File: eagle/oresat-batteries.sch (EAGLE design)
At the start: 73 parts, among them IC1 74AHC1G08DBV, U1 TCAN330, U2 STM32F042K6, U3 ADP5062, X1 16MHz

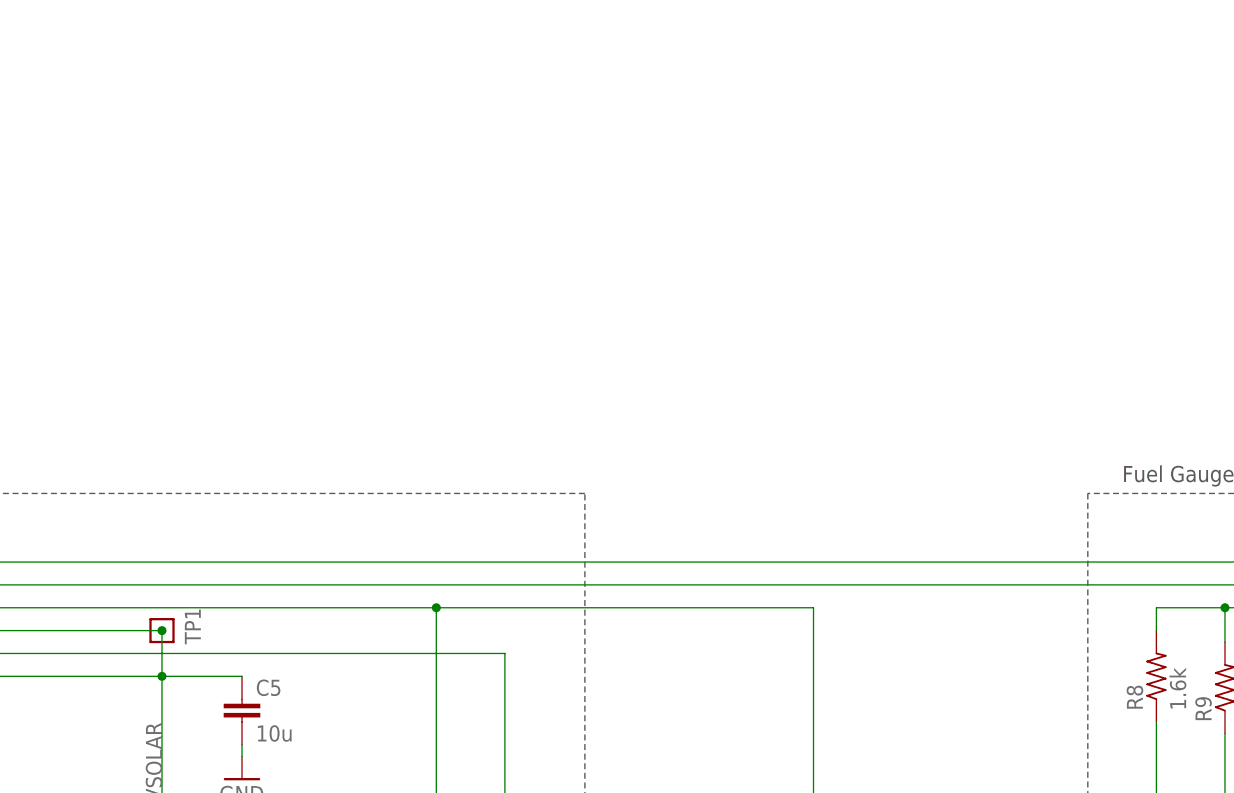
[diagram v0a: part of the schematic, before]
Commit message: Added 3.3V switching power supply
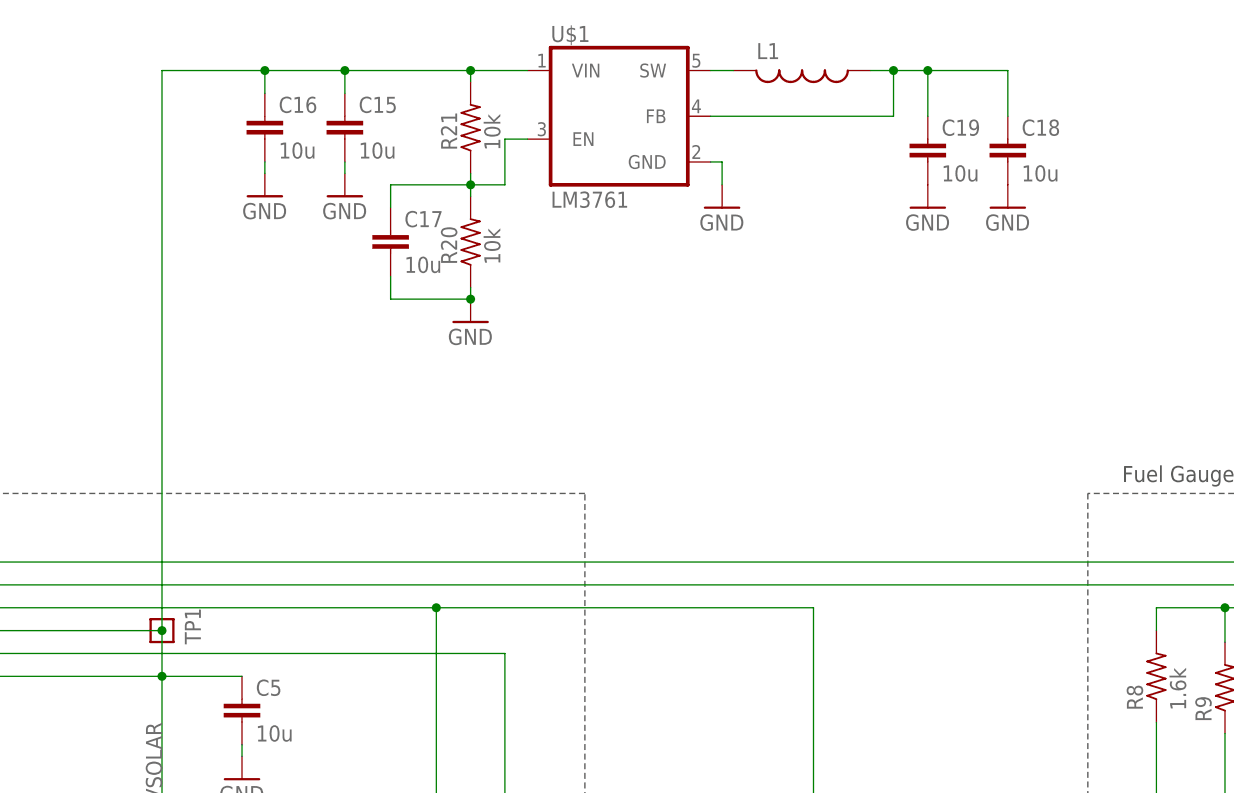
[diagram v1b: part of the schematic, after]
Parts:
- added C15, C16, C17, C18, C19: 10u, rcl:C-EUC0805
- added L1: (no value), rcl:L-USL2012C
- added R20, R21: 10k, rcl:R-US_R0603
- added U$1: LM3761, oresat-batteries:LM3761
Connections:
- new net N$1: L1.2, U$1.SW
- new net N$3: C18.1, C19.1, L1.1, U$1.FB
- new net N$7: C17.1, R20.2, R21.1, U$1.EN
- net GND: now also C15.2, C16.2, C17.2, C18.2, C19.2, R20.1, U$1.GND
- net VSOLAR: now also C15.1, C16.1, R21.2, U$1.VIN
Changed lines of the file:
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@@
 <part name="GND35" library="supply1" deviceset="GND" device=""/>
 <part name="TP5" library="oresat-batteries" deviceset="TP" device=""/>
+<part name="U$1" library="oresat-batteries" deviceset="LM3761" device=""/>
+<part name="C15" library="rcl" deviceset="C-EU" device="C0805" value="10u"/>
+<part name="C16" library="rcl" deviceset="C-EU" device="C0805" value="10u"/>
+<part name="GND36" library="supply1" deviceset="GND" device=""/>
+<part name="GND37" library="supply1" deviceset="GND" device=""/>
+<part name="C17" library="rcl" deviceset="C-EU" device="C0805" value="10u"/>
+<part name="R20" library="rcl" deviceset="R-US_" device="R0603" value="10k"/>
+<part name="R21" library="rcl" deviceset="R-US_" device="R0603" value="10k"/>
+<part name="GND38" library="supply1" deviceset="GND" device=""/>
+<part name="GND39" library="supply1" deviceset="GND" device=""/>
+<part name="C18" library="rcl" deviceset="C-EU" device="C0805" value="10u"/>
+<part name="C19" library="rcl" deviceset="C-EU" device="C0805" value="10u"/>
+<part name="GND40" library="supply1" deviceset="GND" device=""/>
+<part name="GND41" library="supply1" deviceset="GND" device=""/>
+<part name="L1" library="rcl" deviceset="L-US" device="L2012C"/>
 </parts>
 <sheets>
@@
 <attribute name="NAME" x="74.93" y="237.49" size="1.778" layer="95"/>
 </instance>
+<instance part="U$1" gate="G$1" x="184.15" y="342.9"/>
+<instance part="C15" gate="G$1" x="153.67" y="342.9"/>
+<instance part="C16" gate="G$1" x="144.78" y="342.9"/>
+<instance part="GND36" gate="1" x="144.78" y="334.01"/>
+<instance part="GND37" gate="1" x="153.67" y="334.01"/>
+<instance part="C17" gate="G$1" x="158.75" y="330.2"/>
+<instance part="R20" gate="G$1" x="167.64" y="328.93" smashed="yes" rot="R90">
+<attribute name="NAME" x="166.1414" y="326.39" size="1.778" layer="95" rot="R90"/>
+<attribute name="VALUE" x="170.942" y="326.39" size="1.778" layer="96" rot="R90"/>
+</instance>
+<instance part="R21" gate="G$1" x="167.64" y="341.63" smashed="yes" rot="R90">
+<attribute name="NAME" x="166.1414" y="339.09" size="1.778" layer="95" rot="R90"/>
+<attribute name="VALUE" x="170.942" y="339.09" size="1.778" layer="96" rot="R90"/>
+</instance>
+<instance part="GND38" gate="1" x="167.64" y="320.04"/>
+<instance part="GND39" gate="1" x="195.58" y="332.74"/>
+<instance part="C18" gate="G$1" x="227.33" y="340.36"/>
+<instance part="C19" gate="G$1" x="218.44" y="340.36"/>
+<instance part="GND40" gate="1" x="218.44" y="332.74"/>
+<instance part="GND41" gate="1" x="227.33" y="332.74"/>
+<instance part="L1" gate="G$1" x="204.47" y="347.98" rot="R270"/>
 </instances>
 <busses>
@@
 <pinref part="R19" gate="G$1" pin="1"/>
 <pinref part="GND35" gate="1" pin="GND"/>
+</segment>
+<segment>
+<pinref part="C16" gate="G$1" pin="2"/>
+<pinref part="GND36" gate="1" pin="GND"/>
+<wire x1="144.78" y1="336.55" x2="144.78" y2="337.82" width="0.1524" layer="91"/>
+</segment>
+<segment>
+<pinref part="C15" gate="G$1" pin="2"/>
+<pinref part="GND37" gate="1" pin="GND"/>
+<wire x1="153.67" y1="336.55" x2="153.67" y2="337.82" width="0.1524" layer="91"/>
+</segment>
+<segment>
+<pinref part="R20" gate="G$1" pin="1"/>
+<pinref part="GND38" gate="1" pin="GND"/>
+<wire x1="167.64" y1="323.85" x2="167.64" y2="322.58" width="0.1524" layer="91"/>
+<pinref part="C17" gate="G$1" pin="2"/>
+<wire x1="167.64" y1="322.58" x2="158.75" y2="322.58" width="0.1524" layer="91"/>
+<wire x1="158.75" y1="322.58" x2="158.75" y2="325.12" width="0.1524" layer="91"/>
+<junction x="167.64" y="322.58"/>
+</segment>
+<segment>
+<pinref part="C19" gate="G$1" pin="2"/>
+<pinref part="GND40" gate="1" pin="GND"/>
+</segment>
+<segment>
+<pinref part="C18" gate="G$1" pin="2"/>
+<pinref part="GND41" gate="1" pin="GND"/>
+</segment>
+<segment>
+<pinref part="GND39" gate="1" pin="GND"/>
+<wire x1="195.58" y1="335.28" x2="195.58" y2="337.82" width="0.1524" layer="91"/>
+<pinref part="U$1" gate="G$1" pin="GND"/>
+<wire x1="195.58" y1="337.82" x2="194.31" y2="337.82" width="0.1524" layer="91"/>
 </segment>
 </net>
@@
 <junction x="81.28" y="265.43"/>
 <wire x1="81.28" y1="265.43" x2="81.28" y2="280.67" width="0.1524" layer="91"/>
+<wire x1="133.35" y1="285.75" x2="133.35" y2="347.98" width="0.3048" layer="91"/>
+<pinref part="U$1" gate="G$1" pin="VIN"/>
+<pinref part="C16" gate="G$1" pin="1"/>
+<wire x1="173.99" y1="347.98" x2="167.64" y2="347.98" width="0.3048" layer="91"/>
+<wire x1="167.64" y1="347.98" x2="153.67" y2="347.98" width="0.3048" layer="91"/>
+<wire x1="153.67" y1="347.98" x2="144.78" y2="347.98" width="0.3048" layer="91"/>
+<wire x1="144.78" y1="347.98" x2="144.78" y2="345.44" width="0.1524" layer="91"/>
+<pinref part="C15" gate="G$1" pin="1"/>
+<wire x1="153.67" y1="347.98" x2="153.67" y2="345.44" width="0.1524" layer="91"/>
+<junction x="153.67" y="347.98"/>
+<pinref part="R21" gate="G$1" pin="2"/>
+<wire x1="167.64" y1="347.98" x2="167.64" y2="346.71" width="0.1524" layer="91"/>
+<junction x="167.64" y="347.98"/>
+<wire x1="133.35" y1="347.98" x2="144.78" y2="347.98" width="0.1524" layer="91"/>
+<junction x="144.78" y="347.98"/>
 </segment>
 </net>
@@
 </segment>
 </net>
+<net name="N$1" class="0">
+<segment>
+<pinref part="U$1" gate="G$1" pin="SW"/>
+<pinref part="L1" gate="G$1" pin="2"/>
+<wire x1="194.31" y1="347.98" x2="196.85" y2="347.98" width="0.1524" layer="91"/>
+</segment>
+</net>
+<net name="N$3" class="0">
+<segment>
+<pinref part="U$1" gate="G$1" pin="FB"/>
+<wire x1="194.31" y1="342.9" x2="214.63" y2="342.9" width="0.1524" layer="91"/>
+<wire x1="214.63" y1="342.9" x2="214.63" y2="347.98" width="0.1524" layer="91"/>
+<pinref part="L1" gate="G$1" pin="1"/>
+<wire x1="214.63" y1="347.98" x2="212.09" y2="347.98" width="0.1524" layer="91"/>
+<wire x1="214.63" y1="347.98" x2="218.44" y2="347.98" width="0.1524" layer="91"/>
+<junction x="214.63" y="347.98"/>
+<pinref part="C19" gate="G$1" pin="1"/>
+<wire x1="218.44" y1="347.98" x2="218.44" y2="342.9" width="0.1524" layer="91"/>
+<wire x1="218.44" y1="347.98" x2="227.33" y2="347.98" width="0.1524" layer="91"/>
+<junction x="218.44" y="347.98"/>
+<pinref part="C18" gate="G$1" pin="1"/>
+<wire x1="227.33" y1="347.98" x2="227.33" y2="342.9" width="0.1524" layer="91"/>
+</segment>
+</net>
+<net name="N$7" class="0">
+<segment>
+<pinref part="R21" gate="G$1" pin="1"/>
+<pinref part="R20" gate="G$1" pin="2"/>
+<wire x1="167.64" y1="336.55" x2="167.64" y2="335.28" width="0.1524" layer="91"/>
+<pinref part="C17" gate="G$1" pin="1"/>
+<wire x1="167.64" y1="335.28" x2="167.64" y2="334.01" width="0.1524" layer="91"/>
+<wire x1="158.75" y1="332.74" x2="158.75" y2="335.28" width="0.1524" layer="91"/>
+<wire x1="158.75" y1="335.28" x2="167.64" y2="335.28" width="0.1524" layer="91"/>
+<junction x="167.64" y="335.28"/>
+<wire x1="167.64" y1="335.28" x2="171.45" y2="335.28" width="0.1524" layer="91"/>
+<wire x1="171.45" y1="335.28" x2="171.45" y2="340.36" width="0.1524" layer="91"/>
+<pinref part="U$1" gate="G$1" pin="EN"/>
+<wire x1="171.45" y1="340.36" x2="173.99" y2="340.36" width="0.1524" layer="91"/>
+</segment>
+</net>

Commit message: First cleanup of batteries post-Austin going to NASA. Austiiiiinnnnnnnnn, come backgit diff ../design.mdn111git diff ../design.mdn./run More sane two sheet layout on schematic, cleaned up in and out arrays but it needs more thought. New OreSat card board and connector.
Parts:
- removed C12, C13: 100n, rcl:C-EUC0603
- removed C15, C19: 10u, rcl:C-EUC0805
- removed CF1: ORESAT-CONNECTOR-40PIN, low-gain-radio:ORESAT-CONNECTOR-40PIN
- removed CF2: 2MM-RA-1X8, oresat-batteries:2MM-RA-1X8
- removed DEBUG_DNP: (no value), pinhead:PINHD-2X8
- removed L1: (no value), rcl:L-USL2012C
- removed LED1: DNP/GRN, led:LEDCHIPLED_0603
- removed U$1: LM3761, oresat-batteries:LM3761
- removed U$10, U$11, U$12, U$15, U$16, U$17, U$18, U$19, U$22, U$23, U$25, U$26, U$27, U$28, U$29, U$4, U$8, U$9: TP, oresat-batteries:TP
- removed U$13, U$14, U$20: CSD16340Q3, oresat-batteries:CSD16340Q3
- removed U$2: BQ2970, oresat-batteries:BQ2970
- removed U$21: 4.19, oresat-batteries:RES_HEATER
- removed U$3: 2AHBATT, oresat-batteries:2AHBATT
- removed U$5: STC3100LST, oresat-batteries:STC3100LST
- added B1: 2AHBATT, oresat-batteries:2AHBATT
- added C22: 100n, rcl_custom:C-EU0402-B-NOSILK
- added C25: 22u, oresat-rcl:C-EU0805-B-NOSILK
- added CARD: ORESAT-CARD-V0.5, oresat-card:ORESAT-CARD-V0.5
- added D1, D3: GREEN, SparkFun-LED:LED-GREEN0603
- added F1: 2016L200PR, F-LITTELFUSE-2016L-SERIES-PTC:F-LITTELFUSE-2016L-SERIES-PTC
- added F2: 2016L500DR, F-LITTELFUSE-2016L-SERIES-PTC:F-LITTELFUSE-2016L-SERIES-PTC
- added H1, H2, H3, H4: STAND-OFFTIGHT, SparkFun-Hardware:STAND-OFFTIGHT
- added J5: (no value), SparkFun-Connectors:6_PIN_SERIAL_TARGETSILK
- added J6: J-SAMTEC-TFM-120-X1-XXX-D-RA, J-Samtec-TFM-120-X1-XXX-D-RA:J-SAMTEC-TFM-120-X1-XXX-D-RA
- added J7: 1.27MM-SWD-CONNECTOR, J-CNC-3220-10-0100-00-ARM-SWD-port:1.27MM-SWD-CONNECTOR
- added JP8: (no value), pinhead:PINHD-1X2
- added L3: 1.5 uH, L-Coilcraft-XFL4020:L-COILCRAFT-XFL4020
- added Q1, Q2, Q7: CSD16340Q3, oresat-batteries:CSD16340Q3
- added Q3, Q4, Q5, Q6: TPN4R712MD, tpn4r712md-pmosfet:TPN4R712MD
- added R22, R23, R24, R25: 470k, rcl:R-US_R0603
- added R26, R28, R29: 10k, rcl:R-US_R0603
- added TP10, TP11, TP12, TP13, TP14, TP16, TP17, TP20, TP6, TP7, TP8, TP9: TP, oresat-batteries:TP
- added TP15: TEST-POINT, Tova:TEST-POINT
- added U10, U12, U13, U9: LTC4412, ltc4412:LTC4412
- added U11: MAX17055, max17055:MAX17055
- added U4, U5, U7, U8: LTC4411, ltc4411:LTC4411
- added U6: STM32F042K6, STM32F042K:STM32F042K6
- C10: value 100n -> .1u
- C11: value 100n -> 20p; device rcl:C-EUC0603 -> rcl_custom:C-EU0402-B-NOSILK; DIS (none) -> Digi-Key; DPN (none) -> 1276-6601-1-ND; MFR (none) -> Samsung; MPN (none) -> CL05C200JB51PNC
- C14: value .1u -> 22u; device rcl:C-EUC0603 -> oresat-rcl:C-EU0603-B-NOSILK; DIS (none) -> Digi-Key; DPN (none) -> 1276-1001-1-ND; MFR (none) -> Samsung; MPN (none) -> CL05B104KO5NNNC
- C16: value 10u -> 20p; device rcl:C-EUC0805 -> rcl_custom:C-EU0402-B-NOSILK; DIS (none) -> Digi-Key; DPN (none) -> 1276-6601-1-ND; MFR (none) -> Samsung; MPN (none) -> CL05C200JB51PNC
- C17, C5: value 10u -> 100n; device rcl:C-EUC0805 -> rcl_custom:C-EU0402-B-NOSILK; DIS (none) -> Digi-Key; DPN (none) -> 1276-1001-1-ND; MFR (none) -> Samsung; MPN (none) -> CL05B104KO5NNNC
- C18: value 10u -> 22u; device rcl:C-EUC0805 -> oresat-rcl:C-EU0805-B-NOSILK
- C2: value 22u -> .47u; device rcl:C-EUC1206 -> rcl:C-EUC0603
- C3: value 22u -> 100n; device rcl:C-EUC1206 -> rcl_custom:C-EU0402-B-NOSILK; DIS (none) -> Digi-Key; DPN (none) -> 1276-1001-1-ND; MFR (none) -> Samsung; MPN (none) -> CL05B104KO5NNNC
- C4: value 10n -> 10u; device rcl:C-EUC0603 -> oresat-rcl:C-EU0603-B-NOSILK; DIS (none) -> Digi-Key; DPN (none) -> 1276-1001-1-ND; MFR (none) -> Samsung; MPN (none) -> CL05B104KO5NNNC
- C6: value .22u -> 10u; device rcl:C-EUC0603 -> oresat-rcl:C-EU0805-B-NOSILK
- C7: value 1u -> .1u; device rcl:C-EUC0805 -> rcl:C-EUC0603
- C8: value 20p -> 10u; device rcl:C-EUC0603 -> oresat-rcl:C-EU0805-B-NOSILK
- C9: value 20p -> 100n; device rcl:C-EUC0603 -> rcl_custom:C-EU0402-B-NOSILK; DIS (none) -> Digi-Key; DPN (none) -> 1276-1001-1-ND; MFR (none) -> Samsung; MPN (none) -> CL05B104KO5NNNC
- D2: value BAS40 -> GREEN; device diode:BAS40 -> SparkFun-LED:LED-GREEN0603
- R1: value THERMISTER -> 2.7k; device rcl:R-US_R0603 -> rcl_custom:R-US_0402-B-NOSILK; DIS (none) -> Digi-Key; DPN (none) -> 1276-4275-1-ND; MFR (none) -> Samsung; MPN (none) -> RC1005F6653CS
- R10: value 10k -> 470k; device rcl:R-US_R0603 -> rcl_custom:R-US_0402-B-NOSILK; DIS (none) -> Digi-Key; DPN (none) -> 1276-4275-1-ND; MFR (none) -> Samsung; MPN (none) -> RC1005F6653CS
- R11: value 10k -> 4.7k
- R12: value 10k -> 100k; device rcl:R-US_R0603 -> rcl_custom:R-US_0402-B-NOSILK; DIS (none) -> Digi-Key; DPN (none) -> 1276-4275-1-ND; MFR (none) -> Samsung; MPN (none) -> RC1005F6653CS
- R13: value DNP/0 -> 10k
- R15: value DNP/10k -> 10k; device rcl:R-US_R0603 -> rcl_custom:R-US_0402-B-NOSILK; DIS (none) -> Digi-Key; DPN (none) -> 1276-4275-1-ND; MFR (none) -> Samsung; MPN (none) -> RC1005F6653CS
- R16: value DNP/10K -> NP; device rcl:R-US_R0603 -> rcl_custom:R-US_0402-B-NOSILK; DIS (none) -> Digi-Key; DPN (none) -> 1276-4275-1-ND; MFR (none) -> Samsung; MPN (none) -> RC1005F6653CS
- R17: device rcl:R-US_R0603 -> rcl_custom:R-US_0402-B-NOSILK; DIS (none) -> Digi-Key; DPN (none) -> 1276-4275-1-ND; MFR (none) -> Samsung; MPN (none) -> RC1005F6653CS
- R18: value 10k -> NP; device rcl:R-US_R0603 -> rcl_custom:R-US_0402-B-NOSILK; DIS (none) -> Digi-Key; DPN (none) -> 1276-4275-1-ND; MFR (none) -> Samsung; MPN (none) -> RC1005F6653CS
- R19: value DNP/10k -> 10k
- R2: value 220 -> 2.7k; device rcl:R-US_R0603 -> rcl_custom:R-US_0402-B-NOSILK; DIS (none) -> Digi-Key; DPN (none) -> 1276-4275-1-ND; MFR (none) -> Samsung; MPN (none) -> RC1005F6653CS
- R20: value 10k -> 4.19; device rcl:R-US_R0603 -> oresat-batteries:RES_HEATER
- R3: value .01-.05 -> 2.7k; device rcl:R-US_R0603 -> rcl_custom:R-US_0402-B-NOSILK; DIS (none) -> Digi-Key; DPN (none) -> 1276-4275-1-ND; MFR (none) -> Samsung; MPN (none) -> RC1005F6653CS
- R4: value 200k .1% -> .01-.05; device rcl:R-US_R0603 -> rcl:R-US_R2512
- R5: value 1k -> 2.2k
- R6: value 2.2k -> 330
- R7: value 330 -> 10k; device rcl:R-US_R0603 -> rcl_custom:R-US_0402-B-NOSILK; DIS (none) -> Digi-Key; DPN (none) -> 1276-4275-1-ND; MFR (none) -> Samsung; MPN (none) -> RC1005F6653CS
- R8: value 1.6k -> 4.7k
- R9: value 1.6k -> DNP/0
- TP1, TP2, TP3, TP4, TP5: value TP -> TEST-POINT; device oresat-batteries:TP -> Tova:TEST-POINT
- U1: value TCAN330 -> TPS63070; device oresat-batteries:TCAN330 -> ic-pwr-tps63070x:TPS63070X; DIS (none) -> Digi-Key; DPN (none) -> 296-44874-1-ND; MFR (none) -> TI; MPN (none) -> TPS63070
- U2: value STM32F042K6 -> TCAN330; device oresat-batteries:STM32F042K6 -> TCAN330:TCAN330; DIS (none) -> Digi-Key; DPN (none) -> 296-44211-1-ND; MFR (none) -> Texas Instruments; MPN (none) -> TCAN330GDCNT
- U3: value ADP5062 -> BQ2970; device oresat-batteries:ADP5063 -> oresat-batteries:BQ2970
- X1: value 16MHz -> 16MHZ-2.5x2mm; DIS (none) -> Digi-Key; DPN (none) -> XC2181CT-ND; MFR (none) -> ECS Inc.; MPN (none) -> ECS-160-10-36Q-ES-TR
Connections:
- removed net 3V3: C10.1, C11.1, C12.1, C13.1, DEBUG_DNP.1, DEBUG_DNP.2, R10.2, R8.2, R9.2, U$15.P$1, U$20.D, U1.VCC, U2.VDD, U2.VDDA, U2.VDDIO2
- removed net ADP_CBP: C4.1, U3.CBP
- removed net ADP_LED: LED1.C, U3.ILED
- removed net ADP_THR: R1.2, U3.THR
- removed net BATOUT: CF1.3, D2.C
- removed net CANH: CF1.2, DEBUG_DNP.13, DEBUG_DNP.14, U$12.P$1, U1.CANH
- removed net CANL: CF1.1, DEBUG_DNP.11, DEBUG_DNP.12, U$8.P$1, U1.CANL
- removed net CAN_EN: U1.SHDN, U2.PA10
- removed net CAN_LSTN: U1.S, U2.PA9
- removed net COUT: U$13.G, U$19.P$1, U$2.COUT
- removed net DIG_IO1: R11.1, R15.2, TP3.P$1, U3.DIG_IO1
- removed net DIG_IO2: R16.1, R17.2, TP4.P$1, U3.DIG_IO2
- removed net DIG_IO3: R18.1, R19.2, TP5.P$1, U3.DIG_IO3
- removed net IO0: R10.1, R13.2, U$5.IO0, U$9.P$1
- removed net ISO_S: C3.1, CF1.5, U3.ISO_S
- removed net LEDNP: LED1.A, R2.2
- removed net N$13: U$20.S, U$21.1
- removed net N$2: R12.2, U2.PB8-BOOT0
- removed net N$3: C18.1, C19.1, L1.1, U$1.FB
- removed net N$5: IC1A.I1, U$2.DOUT, U$28.P$1
- removed net N$6: C14.1, IC1P.VCC, R14.1
- removed net N$7: C17.1, R20.2, R21.1, U$1.EN
- removed net OSC_IN: C8.1, U2.PF0-OSC_IN, X1.1
- removed net OSC_OUT: C9.1, U2.PF1-OSC_OUT, X1.2
- removed net ROSC: R4.2, U$5.ROSC
- removed net STC_CG: U$14.S, U$2.VSS, U$3.V-
- removed net STC_IO: R13.1, U2.PB5
- removed net STC_VIN: C6.2, R5.1, U$5.VIN
- removed net STM_DEBUG: CF2.8, U2.PA0
- removed net SYS_EN: TP2.P$1, U2.PB0, U3.SYS_EN
- removed net USART2_RX: CF2.7, DEBUG_DNP.5, DEBUG_DNP.6, U2.PA3
- removed net USART2_TX: CF2.6, DEBUG_DNP.3, DEBUG_DNP.4, U2.PA2
- removed net VBATT+: C2.1, C7.2, CF2.2, D2.A, R5.2, R7.2, U$29.P$1, U$3.V+, U$5.VCC, U3.BAT_SNS, U3.ISO_B
- removed net VSOLAR: C15.1, C16.1, C5.1, CF1.4, DEBUG_DNP.7, DEBUG_DNP.8, R11.2, R16.2, R18.2, R21.2, TP1.P$1, U$1.VIN, U3.VIN
- new net !SHUTDOWN: J6.7, J6.8
- new net 3.3V: C14.1, C17.2, C18.1, C22.2, C25.1, C3.2, C9.2, J7.VTREF, R10.2, R11.2, R13.2, R16.2, R2.2, R22.1, R23.1, R24.1, R25.1, R8.2, TP1.1, U1.VOUT, U2.VCC, U6.VDD, U6.VDDA, U6.VDDIO2
- new net 4411MB: U7.OUT, U8.IN
- new net 4411_MT: U4.OUT, U5.IN
- new net ALERT: R13.1, R9.2, TP17.P$1, U11.ALRT
- new net BATT-: B1.V-, IC1P.GND, Q1.S, TP20.P$1, U3.VSS
- new net BGDOUT: IC1A.I1, TP10.P$1, U3.DOUT
- new net BOOT: R17.2, TP15.1, U6.PB8-BOOT0
- new net BQCOUT: Q2.G, TP9.P$1, U3.COUT
- new net CAN_H: J6.3, J6.4, U2.CANH
- new net CAN_L: J6.1, J6.2, U2.CANL
- new net CAN_SHDN: U2.SHDN, U6.PA10
- new net CAN_SILENT: U2.S, U6.PA9
- new net CHARGE-STAT-U4-U5: R25.2, U4.STAT, U5.STAT
- new net CHARGE-STAT-U7-U8: R24.2, U7.STAT, U8.STAT
- new net CHARGE_ENABLE: R29.2, TP11.P$1, U4.CTL, U5.CTL, U7.CTL, U8.CTL
- new net CRYSTALIN: C16.1, U6.PF0-OSC_IN, X1.1
- new net CRYSTALOUT: C11.1, U6.PF1-OSC_OUT, X1.2
- new net DISCHARGE-STAT-U10-U13: R23.2, U12.STAT, U9.STAT
- new net DISCHARGE-STAT-U9-U12: R22.2, U10.STAT, U13.STAT
- new net DISCHARGE_ENABLE: R26.1, TP14.P$1, U10.CTL, U12.CTL, U13.CTL, U9.CTL
- new net INFUSE: F1.P$1, U4.IN, U7.IN
- new net MAX_IO: R9.1
- new net N$270: D1.A, R1.1
- new net N$271: D2.A, R2.1
- new net N$406: J5.VCC, JP8.2
- new net N$435: Q7.S, R20.1
- new net N$436: Q5.G, U12.GATE
- new net N$437: Q3.S, Q5.D, U12.VIN, U9.SENSE
- new net N$438: Q3.G, U9.GATE
- new net N$439: Q6.G, U13.GATE
- new net N$440: Q4.S, Q6.D, U10.SENSE, U13.VIN
- new net N$441: Q4.G, U10.GATE
- new net OUTFUSE: F2.P$2, Q5.S, Q6.S, U12.SENSE, U13.SENSE
- new net PA0: R3.2, U6.PA0
- new net PA1: U6.PA1
- new net PA15: U6.PA15
- new net PA2/USART2_TX: J5.TXO, U6.PA2
- new net PA3/USART2_RX: J5.RXI, U6.PA3
- new net PA4: U6.PA4
- new net PA5/SPI1_SCK: U6.PA5
- new net PA6/SPI1_MISO: U6.PA6
- new net PA7/SPI1_MOSI: U6.PA7
- new net PB0: U6.PB0
- new net PB1: U6.PB1
- new net PB3: U6.PB3
- new net PB4: U6.PB4
- new net PB5: U6.PB5
- new net PB6/SCL: U6.PB6
- new net PB7/SDA: U6.PB7
- new net REG: C2.1, U11.REG
- new net SPARE1: J6.17, J6.18
- new net SPARE10: J6.35, J6.36
- new net SPARE11: J6.37, J6.38
- new net SPARE12: J6.39, J6.40
- new net SPARE2: J6.19, J6.20
- new net SPARE3: J6.21, J6.22
- new net SPARE4: J6.23, J6.24
- new net SPARE5: J6.25, J6.26
- new net SPARE6: J6.27, J6.28
- new net SPARE7: J6.29, J6.30
- new net SPARE8: J6.31, J6.32
- new net SPARE9: J6.33, J6.34
- new net SYSSHD: IC1A.I0, R14.2, TP8.P$1
- new net TEMPSENSE: R19.1, R21.2, U11.AIN
- new net THRM: R19.2, U11.THRM
- new net TPS-EN1: R18.2, R7.1, TP5.1, U1.EN, U1.PS/SYNC
- new net TPS-FB1: R10.1, R12.2, U1.FB
- new net TPS-FB3: TP3.1, U1.FB2
- new net TPS-L3: L3.1, U1.L1
- new net TPS-L4: L3.2, U1.L2
- new net TPS-PG1: R16.1, TP2.1, U1.PG
- new net TPS-VAUX1: C5.1, U1.VAUX
- new net TPS-VSEL1: R15.2, TP4.1, U1.VSEL
- new net VBUS: C4.1, C6.1, C8.1, F1.P$2, F2.P$1, J6.13, J6.14, J6.15, J6.16, JP8.1, R1.2, R7.2, U1.VIN
- new net V_BATT: B1.V+, C10.1, C7.1, IC1P.VCC, Q3.D, Q4.D, Q7.D, R14.1, R28.2, R6.2, TP12.P$1, U10.VIN, U11.BATT, U5.OUT, U8.OUT, U9.VIN
- net ANDDRIVE: now also Q1.G; no longer U$14.G
- net BETSHUT: now also Q1.D, Q2.D; no longer U$13.D, U$14.D
- net BQBAT: now also R6.1, TP6.P$1, U3.BAT; no longer CF1.6, IC1A.I0, R14.2, R7.1, U$2.BAT, U$26.P$1, U$4.P$1
- net BQVMIN: now also R5.1, U3.V-; no longer R6.1, U$2.V-
- net CAN_RX: now also U2.RXD, U6.PA11; no longer U1.RXD, U2.PA11
- net CAN_TX: now also U2.TXD, U6.PA12; no longer U1.TXD, U2.PA12
- net C_SENSE: now also Q2.S, R21.1, R4.2, R5.2, TP13.P$1, U11.CSP; no longer R3.2, U$13.S, U$18.P$1, U$5.CG
- net GND: now also C17.1, C22.1, C25.2, C3.1, C6.2, C7.2, C9.1, D1.C, D2.C, D3.C, J5.GND, J6.10, J6.11, J6.12, J6.5, J6.6, J6.9, J7.GND, J7.GND@2, J7.GNDDET, R18.1, R20.2, R26.2, R29.1, U1.PGND, U10.GND, U11.CSN, U12.GND, U13.GND, U2.GND, U4.GND, U5.GND, U6.VSS, U7.GND, U8.GND, U9.GND; no longer C12.2, C13.2, C15.2, C17.2, C19.2, C3.2, C6.1, C7.1, C9.2, CF2.1, DEBUG_DNP.15, DEBUG_DNP.16, IC1P.GND, R1.1, R19.1, R2.1, R20.1, R3.1, R6.2, U$1.GND, U$16.P$1, U$17.P$1, U$21.2, U$22.P$1, U$23.P$1, U$5.GND, U2.VSS, U3.AGND
- net HEAT: now also Q7.G, R28.1; no longer U$20.G, U2.PA1
- net N$1: now also D3.A, R3.1; no longer L1.2, U$1.SW
- net NRESET: now also J7.!RESET, U6.NRST; no longer CF2.3, U$25.P$1, U2.NRST
- net PA8: now also U6.PA8; no longer U$27.P$1, U2.PA8
- net SCL: now also R11.1, TP7.P$1, U11.SCL; no longer R9.1, U$10.P$1, U$5.SCL, U2.PB6, U3.SCL
- net SDA: now also TP16.P$1, U11.SDA; no longer U$11.P$1, U$5.SDA, U2.PB7, U3.SDA
- net SWCLK: now also J7.SWDCLK/TCK, U6.PA14-SWCLK; no longer CF2.4, U2.PA14-SWCLK
- net SWDIO: now also J7.SWDIO/TMS, U6.PA13-SWDIO; no longer CF2.5, U2.PA13-SWDIO
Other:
- note added: "0603"
- note added: "0805"
- note added: "1.1"
- note added: "10 pn 1.27mm ARM SWD connector"
- note added: "2A cont, 4A trip"
- note added: "5A cont, 10A trip"
- note added: "All caps are ceramic 10% X5R >= 16V Vwv unless marked"
- note added: "All resistors 0402 +/- 1% unless marked"
- note added: "CAN Transceiver"
- note added: "CHANGE ME: CHANGE TO P CHANNEL"
- note added: "CHECK BODY DIODES"
- note added: "Input current: - 4 x 250 mA = 1 A from solar - Inrush from batteries with higher voltage - External chargers (1C only)"
- note added: "Iq = 10uA"
- note added: "Iq = 4uA"
- note added: "Low = Charge"
- note added: "Low = on"
- note added: "Main OreSat Card Connector"
- note added: "Meant for FTDI TTL-232R-3V3 cable"
- note added: "NRST pull-up built in"
- note added: "OreSat Proto-Card"
- note added: "Output curent: - < 100 mA in standby - < 2 A in 70 cm TX - < 5 A in S Band TX"
- note added: "PCB TRACE HEATER"
- note added: "Power VBUS from USB 5V (DEV ONLY)"
- note added: "REPLACE with 0 ohm for flight?"
- note added: "Thermister"
- note added: "Vbus = (3.0, 3.6, 4.2) V"
- note removed: "Battery Charger"
- note removed: "CANH"
- note removed: "CANL"
- note removed: "CAN_EN"
- note removed: "CAN_LSTN"
- note removed: "CAN_RX"
- note removed: "CAN_TX"
- note removed: "DEBUG"
- note removed: "Fix U$ names"
- note removed: "GND"
- note removed: "Ground Pins"
- note removed: "PLACE BY BATTERY"
- note removed: "SCL"
- note removed: "SDA"
- note removed: "STM Microcontroller"
- note removed: "SWCLK"
- note removed: "SWDIO"
- note removed: "SYS_EN"
- note removed: "Two options for a switch on the layout in case NANO racks doesn't like our shutoff"
- note removed: "UARTRX"
- note removed: "UARTX"
- note removed: "USART2_RX"
- note removed: "USART2_TX"
- note removed: "VBATT+"
- note removed: "VSOLAR"
- note removed: "add ground pin clips NP"
